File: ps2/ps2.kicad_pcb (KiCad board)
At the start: 2 copper layers, 135.9 x 48.9 mm, 40 parts, among them J1 keyboard, J2 perslot1a, J3 perslot1b, Q1 Q_NPN_CBE, Q2 Q_PNP_EBC, U1 74HC74, U10 74HC280, U11 74HC541, U2 74HC08, U3 74HC14, U4 74HC05, U5 74HC688, U6 74HC195, U7 74HC195, U8 74HC195, U9 74HC541

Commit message: applied sf68 & ps2 fixes stash from master
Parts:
- R7: value 20k -> 4k7
- moved R4 7.62 mm to (124.5, 81.3), turned to -90 degrees
- moved R8 7.62 mm to (124.5, 73.7), turned to 90 degrees
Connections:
- J1 pad 7: GND -> (no net)
- J1 pad 8: GND -> (no net)
- J1 pad 9: GND -> (no net)
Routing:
- net /DAT: track 65.2 -> 59.4 mm
- net /~{CLK}: track 31.6 -> 36.2 mm
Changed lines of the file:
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@@
 	(footprint "Resistor_THT:R_Axial_DIN0207_L6.3mm_D2.5mm_P2.54mm_Vertical"
 		(layer "F.Cu")
-		(at 124.46 81.28 -90)
+		(at 124.46 73.66 90)
 		(descr "Resistor, Axial_DIN0207 series, Axial, Vertical, pin pitch=2.54mm, 0.25W = 1/4W, length*diameter=6.3*2.5mm^2, http://cdn-reichelt.de/documents/datenblatt/B400/1_4W%23YAG.pdf")
 		(tags "Resistor Axial_DIN0207 series Axial Vertical pin pitch 2.54mm 0.25W = 1/4W length 6.3mm diameter 2.5mm")
 		(property "Reference" "R8"
-			(at -2.54 0 180)
+			(at -2.54 0 0)
 			(layer "F.SilkS")
 			(effects
@@
 		)
 		(property "Value" "4k7"
-			(at 1.27 2.37 90)
+			(at 1.27 2.37 270)
 			(layer "F.Fab")
 			(effects
@@
 		)
 		(property "Datasheet" ""
-			(at 0 0 90)
+			(at 0 0 270)
 			(layer "F.Fab")
 			(hide yes)
@@
 		)
 		(property "Description" ""
-			(at 0 0 90)
+			(at 0 0 270)
 			(layer "F.Fab")
 			(hide yes)
@@
 		)
 		(fp_text user "${REFERENCE}"
-			(at -2.54 0 180)
+			(at -2.54 0 0)
 			(layer "F.Fab")
 			(effects
@@
 		)
 		(pad "1" thru_hole circle
-			(at 0 0 270)
+			(at 0 0 90)
 			(size 1.6 1.6)
 			(drill 0.8)
@@
 		)
 		(pad "2" thru_hole circle
-			(at 2.54 0 270)
+			(at 2.54 0 90)
 			(size 1.6 1.6)
 			(drill 0.8)
@@
 			)
 		)
-		(property "Value" "20k"
+		(property "Value" "4k7"
 			(at 1.27 2.37 90)
 			(layer "F.Fab")
@@
 	(footprint "Resistor_THT:R_Axial_DIN0207_L6.3mm_D2.5mm_P2.54mm_Vertical"
 		(layer "F.Cu")
-		(at 124.46 73.66 90)
+		(at 124.46 81.28 -90)
 		(descr "Resistor, Axial_DIN0207 series, Axial, Vertical, pin pitch=2.54mm, 0.25W = 1/4W, length*diameter=6.3*2.5mm^2, http://cdn-reichelt.de/documents/datenblatt/B400/1_4W%23YAG.pdf")
 		(tags "Resistor Axial_DIN0207 series Axial Vertical pin pitch 2.54mm 0.25W = 1/4W length 6.3mm diameter 2.5mm")
 		(property "Reference" "R4"
-			(at 4.445 0 180)
+			(at 4.445 0 0)
 			(layer "F.SilkS")
 			(effects
@@
 		)
 		(property "Value" "4k7"
-			(at 1.27 2.37 90)
+			(at 1.27 2.37 270)
 			(layer "F.Fab")
 			(effects
@@
 		)
 		(property "Datasheet" ""
-			(at 0 0 90)
+			(at 0 0 270)
 			(layer "F.Fab")
 			(hide yes)
@@
 		)
 		(property "Description" ""
-			(at 0 0 90)
+			(at 0 0 270)
 			(layer "F.Fab")
 			(hide yes)
@@
 		)
 		(fp_text user "${REFERENCE}"
-			(at 4.445 0 180)
+			(at 4.445 0 0)
 			(layer "F.Fab")
 			(effects
@@
 		)
 		(pad "1" thru_hole circle
-			(at 0 0 90)
+			(at 0 0 270)
 			(size 1.6 1.6)
 			(drill 0.8)
@@
 		)
 		(pad "2" thru_hole circle
-			(at 2.54 0 90)
+			(at 2.54 0 270)
 			(size 1.6 1.6)
 			(drill 0.8)
@@
 		)
 		(pad "1" thru_hole circle
-			(at 0 0 90)
+			(at -2.6 0 90)
 			(size 1.509 1.509)
 			(drill 0.97)
@@
 		)
 		(pad "2" thru_hole circle
-			(at -2.6 0 90)
+			(at 0 0 90)
 			(size 1.509 1.509)
 			(drill 0.97)
@@
 		)
 		(pad "3" thru_hole circle
-			(at 2.05 0 90)
+			(at -4.65 0 90)
 			(size 1.509 1.509)
 			(drill 0.97)
@@
 		)
 		(pad "4" thru_hole circle
-			(at -4.65 0 90)
+			(at 2.05 0 90)
 			(size 1.509 1.509)
 			(drill 0.97)
@@
 		)
 		(pad "5" thru_hole circle
-			(at 2.05 2.49 90)
+			(at -4.65 2.49 90)
 			(size 1.509 1.509)
 			(drill 0.97)
@@
 		)
 		(pad "6" thru_hole circle
-			(at -4.65 2.49 90)
+			(at 2.05 2.49 90)
 			(size 1.509 1.509)
 			(drill 0.97)
@@
 			(layers "*.Cu" "*.Mask")
 			(remove_unused_layers no)
-			(net 10 "GND")
 		)
 		(pad "8" thru_hole circle
@@
 			(layers "*.Cu" "*.Mask")
 			(remove_unused_layers no)
-			(net 10 "GND")
 		)
 		(pad "9" thru_hole circle
@@
 			(layers "*.Cu" "*.Mask")
 			(remove_unused_layers no)
-			(net 10 "GND")
 		)
 		(embedded_fonts no)
@@
 	)
 	(segment
-		(start 124.46 66.04)
-		(end 125.73 67.31)
-		(width 0.2)
-		(layer "F.Cu")
-		(net 7)
-	)
-	(segment
 		(start 132.08 66.04)
 		(end 132.08 71.12)
@@
 	)
 	(segment
-		(start 125.73 67.31)
-		(end 125.73 72.39)
+		(start 124.46 81.28)
+		(end 115.98 81.28)
 		(width 0.2)
 		(layer "F.Cu")
@@
 	)
 	(segment
-		(start 124.46 73.66)
-		(end 115.98 73.66)
+		(start 124.46 66.04)
+		(end 125.73 64.77)
 		(width 0.2)
 		(layer "F.Cu")
@@
 	)
 	(segment
-		(start 124.46 66.04)
-		(end 125.73 64.77)
+		(start 130.81 64.77)
+		(end 132.08 66.04)
 		(width 0.2)
 		(layer "F.Cu")
@@
 	)
 	(segment
-		(start 115.98 73.66)
-		(end 115.52 74.12)
+		(start 115.98 81.28)
+		(end 115.52 80.82)
 		(width 0.2)
 		(layer "F.Cu")
@@
 	)
 	(segment
-		(start 125.73 72.39)
-		(end 124.46 73.66)
+		(start 132.08 71.12)
+		(end 128.27 74.93)
 		(width 0.2)
-		(layer "F.Cu")
+		(layer "B.Cu")
 		(net 7)
 	)
 	(segment
-		(start 130.81 64.77)
-		(end 132.08 66.04)
+		(start 128.27 74.93)
+		(end 128.27 77.47)
 		(width 0.2)
-		(layer "F.Cu")
+		(layer "B.Cu")
+		(net 7)
+	)
+	(segment
+		(start 128.27 77.47)
+		(end 124.46 81.28)
+		(width 0.2)
+		(layer "B.Cu")
 		(net 7)
 	)
@@
 	)
 	(segment
-		(start 154.94 81.28)
-		(end 153.67 82.55)
-		(width 0.2)
-		(layer "F.Cu")
-		(net 13)
-	)
-	(segment
-		(start 128.27 67.31)
-		(end 128.27 74.295)
-		(width 0.2)
-		(layer "F.Cu")
-		(net 13)
-	)
-	(segment
-		(start 113.06 76.2)
-		(end 113.03 76.17)
-		(width 0.2)
-		(layer "F.Cu")
-		(net 13)
-	)
-	(segment
-		(start 153.67 82.55)
-		(end 133.35 82.55)
+		(start 126.365 75.565)
+		(end 124.46 73.66)
 		(width 0.2)
 		(layer "F.Cu")
@@
 	)
 	(segment
-		(start 128.27 77.47)
-		(end 124.46 81.28)
+		(start 149.225 75.565)
+		(end 126.365 75.565)
 		(width 0.2)
 		(layer "F.Cu")
@@
 	)
 	(segment
-		(start 128.27 74.295)
-		(end 128.27 77.47)
+		(start 113.03 78.77)
+		(end 119.35 78.77)
 		(width 0.2)
 		(layer "F.Cu")
@@
 	)
 	(segment
-		(start 126.365 76.2)
-		(end 113.06 76.2)
+		(start 129.54 68.58)
+		(end 129.54 66.04)
 		(width 0.2)
 		(layer "F.Cu")
@@
 	)
 	(segment
-		(start 133.35 82.55)
-		(end 128.27 77.47)
+		(start 154.94 81.28)
+		(end 149.225 75.565)
 		(width 0.2)
 		(layer "F.Cu")
@@
 	)
 	(segment
-		(start 126.365 76.2)
-		(end 128.27 74.295)
+		(start 124.46 73.66)
+		(end 129.54 68.58)
 		(width 0.2)
 		(layer "F.Cu")
@@
 	)
 	(segment
-		(start 129.54 66.04)
-		(end 128.27 67.31)
+		(start 124.46 73.66)
+		(end 119.35 78.77)
 		(width 0.2)
 		(layer "F.Cu")

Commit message: [ps2] fixed send request RC constant 	t must be >= 100us 	RC was being t, therefore t was actually smaller than 100us 	RC is now >= 1.28 * 100us (R : 10kohm -> 14.7kohm) 	t ~= 120us >= 100us
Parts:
- R1: value 10k -> 14k7
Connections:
- J1 pad 7: (no net) -> GND
- J1 pad 8: (no net) -> GND
- J1 pad 9: (no net) -> GND
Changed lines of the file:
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@@
 			)
 		)
-		(property "Value" "10k"
+		(property "Value" "14k7"
 			(at 1.27 2.37 90)
 			(layer "F.Fab")
@@
 			(layers "*.Cu" "*.Mask")
 			(remove_unused_layers no)
+			(net 10 "GND")
 		)
 		(pad "8" thru_hole circle
@@
 			(layers "*.Cu" "*.Mask")
 			(remove_unused_layers no)
+			(net 10 "GND")
 		)
 		(pad "9" thru_hole circle
@@
 			(layers "*.Cu" "*.Mask")
 			(remove_unused_layers no)
+			(net 10 "GND")
 		)
 		(embedded_fonts no)

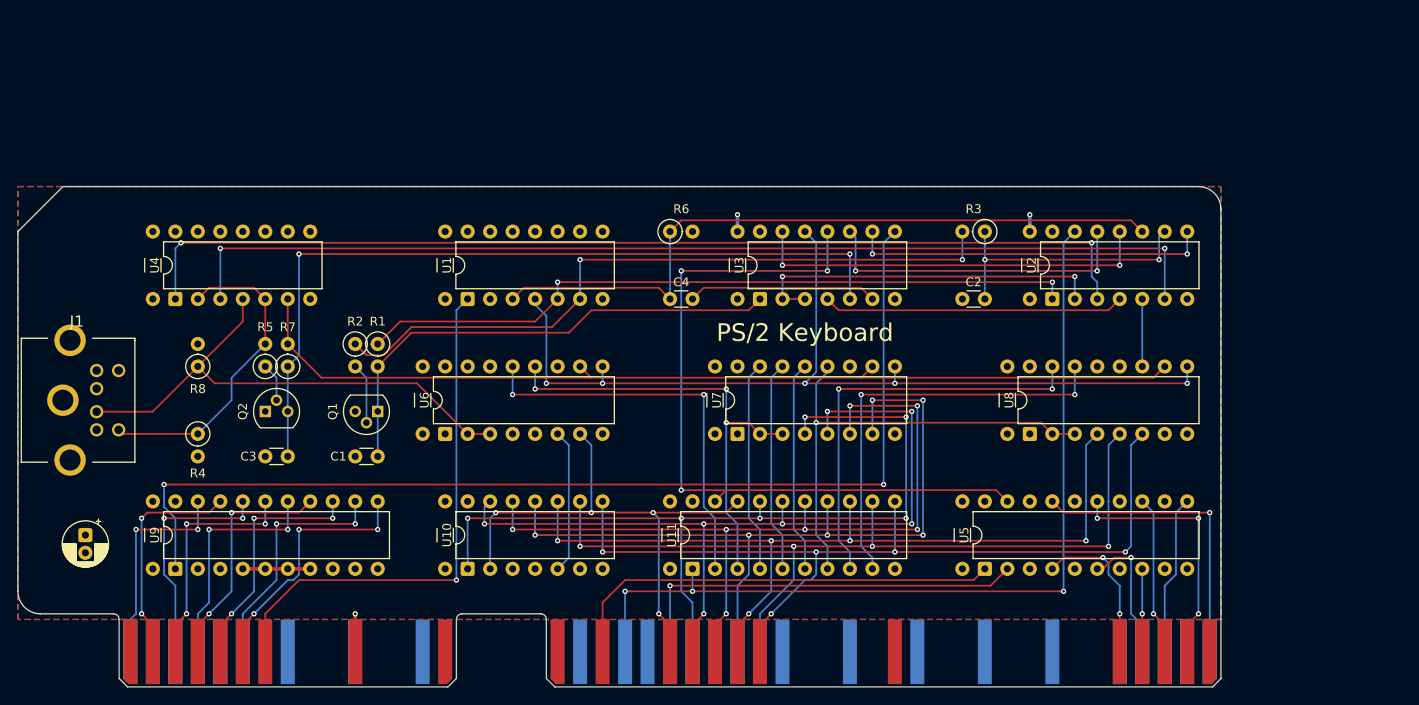
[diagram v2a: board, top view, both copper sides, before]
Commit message: [ps2]:	made pcb design of the new latest schematic
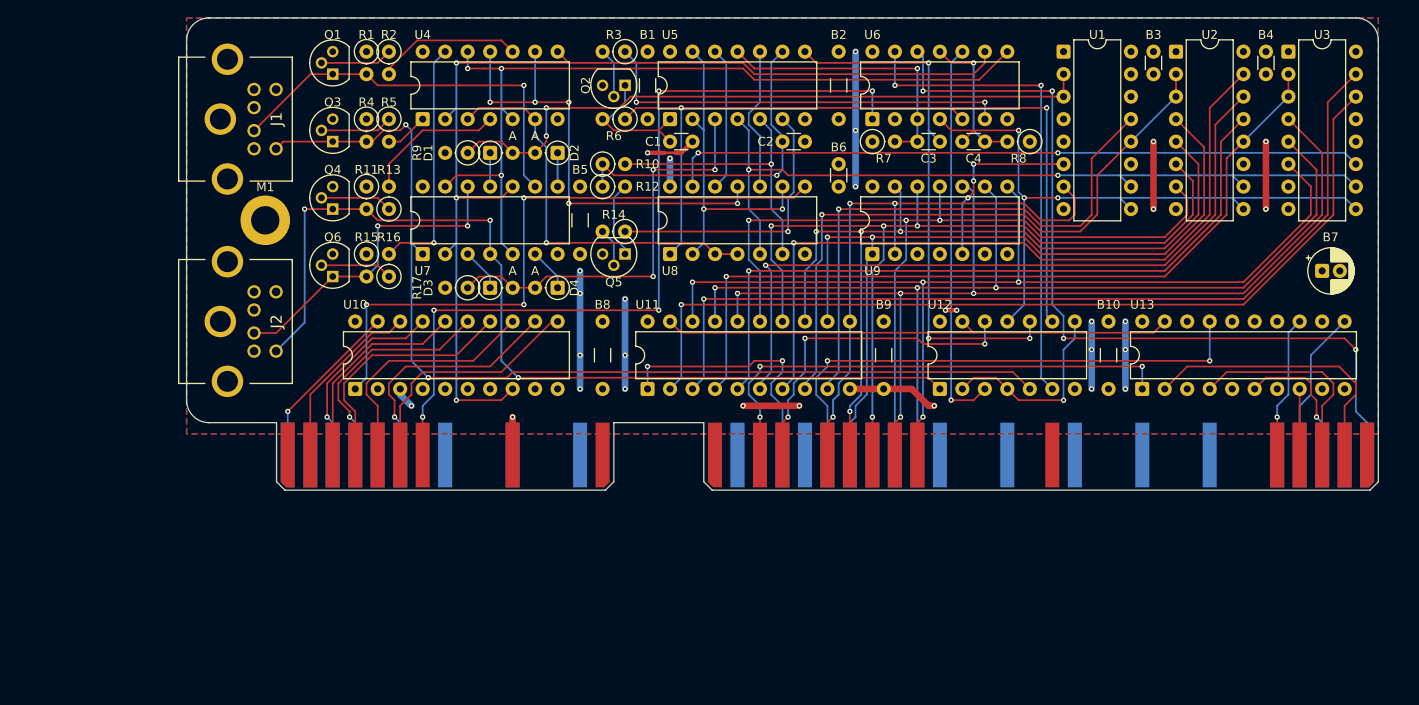
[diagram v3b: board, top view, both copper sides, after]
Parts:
- removed CB1 (x11): C_Disc_D3.0mm_W1.6mm_P7.62mm, Capacitor_THT:C_Disc_D3.0mm_W1.6mm_P7.62mm
- removed CB1: CP_Radial_D5.0mm_P2.00mm, Capacitor_THT:CP_Radial_D5.0mm_P2.00mm
- added B1: 100n, Capacitor_THT:C_Disc_D3.0mm_W1.6mm_P7.62mm, F.Cu at (175.3, 38.1)
- added B10: 100n, Capacitor_THT:C_Disc_D3.0mm_W1.6mm_P7.62mm, F.Cu at (227.3, 68.6)
- added B2: 100n, Capacitor_THT:C_Disc_D3.0mm_W1.6mm_P7.62mm, F.Cu at (196.8, 38.1)
- added B3: 100n, Capacitor_THT:C_Disc_D3.0mm_W1.6mm_P2.54mm, F.Cu at (232.4, 38.1)
- added B4: 100n, Capacitor_THT:C_Disc_D3.0mm_W1.6mm_P2.54mm, F.Cu at (245.1, 38.1)
- added B5: 100n, Capacitor_THT:C_Disc_D3.0mm_W1.6mm_P7.62mm, F.Cu at (167.6, 53.3)
- added B6: 100n, Capacitor_THT:C_Disc_D3.0mm_W1.6mm_P2.54mm, F.Cu at (196.8, 53.3)
- added B7: 10u, Capacitor_THT:CP_Radial_D5.0mm_P2.00mm, F.Cu at (251.5, 62.9)
- added B8: 100n, Capacitor_THT:C_Disc_D3.0mm_W1.6mm_P7.62mm, F.Cu at (170.2, 68.6)
- added B9: 100n, Capacitor_THT:C_Disc_D3.0mm_W1.6mm_P7.62mm, F.Cu at (201.9, 68.6)
- added D1: schotty, Diode_THT:D_DO-35_SOD27_P2.54mm_Vertical_AnodeUp, F.Cu at (157.5, 49.5)
- added D2: schotty, Diode_THT:D_DO-35_SOD27_P2.54mm_Vertical_AnodeUp, F.Cu at (165.1, 49.5)
- added D3: schotty, Diode_THT:D_DO-35_SOD27_P2.54mm_Vertical_AnodeUp, F.Cu at (157.5, 64.8)
- added D4: schotty, Diode_THT:D_DO-35_SOD27_P2.54mm_Vertical_AnodeUp, F.Cu at (165.1, 64.8)
- added J4: perslot1a, Connector_PCBEdge:pcb_edge_60_P2.54_new, F.Cu at (181.6, 80.0)
- added M1: MountingHole_3.2mm_M3_DIN965_Pad, MountingHole:MountingHole_3.2mm_M3_DIN965_Pad, F.Cu at (132.1, 57.1)
- added Q3: BC547B, Package_TO_SOT_THT:TO-92, F.Cu at (139.7, 48.3)
- added Q4: BC547B, Package_TO_SOT_THT:TO-92, F.Cu at (139.7, 55.9)
- added Q5: BC547B, Package_TO_SOT_THT:TO-92, F.Cu at (172.7, 61.0)
- added Q6: BC547B, Package_TO_SOT_THT:TO-92, F.Cu at (139.7, 63.5)
- added R10: 10k, Resistor_THT:R_Axial_DIN0207_L6.3mm_D2.5mm_P2.54mm_Vertical, F.Cu at (170.2, 50.8)
- added R11: 4k7, Resistor_THT:R_Axial_DIN0207_L6.3mm_D2.5mm_P2.54mm_Vertical, F.Cu at (143.5, 53.3)
- added R12: 1k, Resistor_THT:R_Axial_DIN0207_L6.3mm_D2.5mm_P2.54mm_Vertical, F.Cu at (170.2, 53.3)
- added R13: 10k, Resistor_THT:R_Axial_DIN0207_L6.3mm_D2.5mm_P2.54mm_Vertical, F.Cu at (146.1, 55.9)
- added R14: 10k, Resistor_THT:R_Axial_DIN0207_L6.3mm_D2.5mm_P2.54mm_Vertical, F.Cu at (172.7, 58.4)
- added R15: 4k7, Resistor_THT:R_Axial_DIN0207_L6.3mm_D2.5mm_P2.54mm_Vertical, F.Cu at (143.5, 61.0)
- added R16: 10k, Resistor_THT:R_Axial_DIN0207_L6.3mm_D2.5mm_P2.54mm_Vertical, F.Cu at (146.1, 63.5)
- added R17: 10k, Resistor_THT:R_Axial_DIN0207_L6.3mm_D2.5mm_P2.54mm_Vertical, F.Cu at (154.9, 64.8)
- added R9: 10k, Resistor_THT:R_Axial_DIN0207_L6.3mm_D2.5mm_P2.54mm_Vertical, F.Cu at (154.9, 49.5)
- added U12: 74HC32, Package_DIP:DIP-14_W7.62mm, F.Cu at (208.3, 76.2)
- added U13: 74HC688, Package_DIP:DIP-20_W7.62mm, F.Cu at (231.1, 76.2)
- C1: value 10nF -> 10n
- C2: value 22pF -> 10n
- C3: value 10nF -> 220p
- C4: value 22pF -> 22p
- J1: value keyboard -> port0
- J2: value perslot1a -> port1; footprint Connector_PCBEdge:pcb_edge_60_P2.54_new -> Connector_TE-Connectivity:57492651
- Q1: value Q_NPN_CBE -> BC547B
- Q2: value Q_PNP_EBC -> BC547B
- R1: value 14k7 -> 4k7
- R6: value 10k -> 14k7
- R7: value 4k7 -> 1k
- R8: value 4k7 -> 2k
- U1: value 74HC74 -> 74HC195; footprint Package_DIP:DIP-14_W7.62mm -> Package_DIP:DIP-16_W7.62mm
- U10: value 74HC280 -> 74HC541; footprint Package_DIP:DIP-14_W7.62mm -> Package_DIP:DIP-20_W7.62mm
- U2: value 74HC08 -> 74HC195; footprint Package_DIP:DIP-14_W7.62mm -> Package_DIP:DIP-16_W7.62mm
- U3: value 74HC14 -> 74HC195; footprint Package_DIP:DIP-14_W7.62mm -> Package_DIP:DIP-16_W7.62mm
- U4: value 74HC05 -> 74HC02
- U5: value 74HC688 -> 74HC14; footprint Package_DIP:DIP-20_W7.62mm -> Package_DIP:DIP-14_W7.62mm
- U6: value 74HC195 -> 74HC74; footprint Package_DIP:DIP-16_W7.62mm -> Package_DIP:DIP-14_W7.62mm
- U7: value 74HC195 -> 74HC32; footprint Package_DIP:DIP-16_W7.62mm -> Package_DIP:DIP-14_W7.62mm
- U8: value 74HC195 -> 74HC00; footprint Package_DIP:DIP-16_W7.62mm -> Package_DIP:DIP-14_W7.62mm
- U9: value 74HC541 -> 74HC280; footprint Package_DIP:DIP-20_W7.62mm -> Package_DIP:DIP-14_W7.62mm
- moved R8 97.4 mm to (218.4, 48.3), turned to 180 degrees
- moved U9 86.4 mm to (200.7, 61.0)
- moved C3 81.8 mm to (205.7, 48.3)
- moved U1 72.9 mm to (222.2, 38.1), turned to 0 degrees
- moved R7 70.8 mm to (200.7, 48.3), turned to 0 degrees
- moved U3 65.9 mm to (247.7, 38.1), turned to 0 degrees
- moved U5 62.0 mm to (177.8, 45.7)
- moved U6 59.9 mm to (200.7, 45.7)
- moved Q2 54.8 mm to (172.7, 41.9), turned to 180 degrees
- moved C1 50.3 mm to (177.8, 48.3)
- moved J2 48.1 mm to (130.8, 67.3), turned to 90 degrees
- moved R3 45.4 mm to (172.7, 38.1)
- moved U8 45.4 mm to (177.8, 61.0)
- moved U7 41.0 mm to (149.9, 61.0)
- moved R4 40.3 mm to (143.5, 45.7)
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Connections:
- C1 pad 1: GND -> Net-(Q5-C)
- C1 pad 2: Net-(Q1-C) -> GND
- C2 pad 1: GND -> Net-(C4-Pad1)
- C2 pad 2: Net-(C2-Pad2) -> GND
- C3 pad 1: GND -> Net-(U1A-C)
- C3 pad 2: Net-(Q2-C) -> /TBSY
- C4 pad 1: Net-(U1A-C) -> /~{W}
- C4 pad 2: Net-(C4-Pad2) -> Net-(U1B-C)
- J1 pad 1: /DAT -> /DAT_{0}
- J1 pad 5: /~{CLK} -> /~{CLK_{0}}
- J2 pad 1: +5V -> /DAT_{1}
- J2 pad 4: GND -> +5V
- J2 pad 5: /DS.~{U} -> /~{CLK_{1}}
- J2 pad 8: /DIR.~{R} -> GND
- Q1 pad 1: Net-(Q1-C) -> /DAT_{0}
- Q1 pad 2: Net-(Q1-B) -> Net-(Q2-B)
- Q2 pad 1: +5V -> Net-(Q5-C)
- Q2 pad 2: Net-(Q2-B) -> Net-(Q5-B)
- Q2 pad 3: Net-(Q2-C) -> GND
- R1 pad 1: Net-(U1A-Q) -> +5V
- R1 pad 2: Net-(Q1-C) -> /DAT_{0}
- R2 pad 1: Net-(U1A-~{Q}) -> Net-(Q2-B)
- R2 pad 2: Net-(Q1-B) -> Net-(R5-Pad2)
- R3 pad 1: Net-(C2-Pad2) -> Net-(U1A-~{Q})
- R3 pad 2: Net-(U1A-~{Q}) -> Net-(Q5-B)
- R4 pad 1: /~{CLK} -> +5V
- R4 pad 2: +5V -> /~{CLK_{0}}
- R5 pad 1: Net-(Q2-B) -> Net-(Q1-B)
- R5 pad 2: /~{CLK} -> Net-(R4-Pad2)
- R6 pad 1: Net-(U1A-C) -> /SBSY
- R6 pad 2: GND -> Net-(Q5-C)
- R7 pad 1: Net-(Q2-C) -> +5V
- R7 pad 2: /CP -> Net-(U1A-C)
- R8 pad 1: /DAT -> +5V
- R8 pad 2: +5V -> Net-(U1B-C)
- U1 pad 1: /~{RES} -> +5V
- U1 pad 10: +5V -> /CP
- U1 pad 11: GND -> unconnected-(U9-~{Q3}-Pad11)
- U1 pad 12: GND -> /shift_registers/D_{q6}
- U1 pad 13: +5V -> /shift_registers/D_{q7}
- U1 pad 14: +5V -> unconnected-(U9-Q1-Pad14)
- U1 pad 2: GND -> /DAT_{d}
- U1 pad 3: Net-(U1A-C) -> /DAT_{d}
- U1 pad 4: /~{W} -> +5V
- U1 pad 5: Net-(U1A-Q) -> +5V
- U1 pad 6: Net-(U1A-~{Q}) -> /shift_registers/EPAR
- U1 pad 7: GND -> /D_{15}
- U1 pad 8: unconnected-(U1B-~{Q}-Pad8) -> GND
- U1 pad 9: unconnected-(U1B-Q-Pad9) -> /~{W}
- U10 pad 1: /D_{14} -> /~{RCV}
- U10 pad 10: /D_{10} -> GND
- U10 pad 11: /D_{11} -> /IRQ_{0}
- U10 pad 12: /D_{12} -> /IRQ_{1}
- U10 pad 13: /D_{13} -> /IRQ_{2}
- U10 pad 14: +5V -> /IRQ_{3}
- U10 pad 2: /D_{15} -> GND
- U10 pad 3: unconnected-(U10-NC-Pad3) -> +5V
- U10 pad 5: /PAR -> GND
- U10 pad 6: unconnected-(U10-Odd-Pad6) -> GND
- U10 pad 8: /D_{8} -> /PORT
- U10 pad 9: /D_{9} -> +5V
- U11 pad 11: /D_{8} -> /D_{15}
- U11 pad 12: /D_{9} -> /D_{14}
- U11 pad 13: /D_{10} -> /D_{13}
- U11 pad 14: /D_{11} -> /D_{12}
- U11 pad 15: /D_{12} -> /D_{11}
- U11 pad 16: /D_{13} -> /D_{10}
- U11 pad 17: /D_{14} -> /D_{9}
- U11 pad 18: /D_{15} -> /D_{8}
- U11 pad 2: /DQ_{7} -> /shift_registers/D_{q0}
- U11 pad 3: /DQ_{6} -> /shift_registers/D_{q1}
- U11 pad 4: /DQ_{5} -> /shift_registers/D_{q2}
- U11 pad 5: /DQ_{4} -> /shift_registers/D_{q3}
- U11 pad 6: /DQ_{3} -> /shift_registers/D_{q4}
- U11 pad 7: /DQ_{2} -> /shift_registers/D_{q5}
- U11 pad 8: /DQ_{1} -> /shift_registers/D_{q6}
- U11 pad 9: /DQ_{0} -> /shift_registers/D_{q7}
- U2 pad 1: Net-(U1A-Q) -> +5V
- U2 pad 10: Net-(U1A-C) -> /CP
- U2 pad 11: Net-(U2-Pad11) -> unconnected-(U10-~{Q3}-Pad11)
- U2 pad 12: Net-(U2-Pad12) -> /shift_registers/D_{q2}
- U2 pad 13: /DIR.~{R} -> /shift_registers/D_{q3}
- U2 pad 14: +5V -> /shift_registers/D_{q4}
- U2 pad 2: Net-(U2-Pad2) -> /shift_registers/D_{q6}
- U2 pad 3: Net-(U2-Pad3) -> /shift_registers/D_{q6}
- U2 pad 4: Net-(U2-Pad4) -> /D_{14}
- U2 pad 5: /~{DQO} -> /D_{13}
- U2 pad 6: Net-(U2-Pad6) -> /D_{12}
- U2 pad 7: GND -> /D_{11}
- U2 pad 8: Net-(U2-Pad8) -> GND
- U2 pad 9: Net-(C2-Pad2) -> /~{W}
- U3 pad 1: Net-(Q1-C) -> +5V
- U3 pad 10: Net-(U2-Pad12) -> /CP
- U3 pad 11: /~{S} -> /~{D_{q}}
- U3 pad 12: /~{W} -> unconnected-(U11-Q3-Pad12)
- U3 pad 13: Net-(U2-Pad11) -> unconnected-(U11-Q2-Pad13)
- U3 pad 14: +5V -> /shift_registers/D_{q0}
- U3 pad 2: Net-(U2-Pad2) -> /shift_registers/D_{q2}
- U3 pad 3: Net-(U2-Pad2) -> /shift_registers/D_{q2}
- U3 pad 4: Net-(U2-Pad4) -> /D_{10}
- U3 pad 5: Net-(Q2-C) -> /D_{9}
- U3 pad 6: Net-(C4-Pad2) -> /D_{8}
- U3 pad 8: /~{RCV} -> GND
- U3 pad 9: Net-(U2-Pad8) -> /~{W}
- U4 pad 1: Net-(U2-Pad3) -> Net-(R4-Pad2)
- U4 pad 10: unconnected-(U4-Pad10) -> Net-(R5-Pad2)
- U4 pad 11: GND -> /DAT_{h}
- U4 pad 12: unconnected-(U4-Pad12) -> /ports_mux/~{P_{1}}
- U4 pad 13: GND -> Net-(R11-Pad2)
- U4 pad 2: /~{CLK} -> /PORT
- U4 pad 3: Net-(U2-Pad6) -> /~{CLK_{h}}
- U4 pad 4: /DAT -> Net-(R10-Pad2)
- U4 pad 5: /~{CLK} -> /ports_mux/~{P_{1}}
- U4 pad 6: /CP -> /~{CLK_{h}}
- U4 pad 8: unconnected-(U4-Pad8) -> /PORT
- U4 pad 9: GND -> /DAT_{h}
- U5 pad 1: /DS.~{U} -> Net-(Q5-C)
- U5 pad 10: GND -> Net-(U7-Pad10)
- U5 pad 11: /A_{4} -> Net-(U1A-C)
- U5 pad 12: GND -> Net-(U7-Pad12)
- U5 pad 13: /A_{3} -> Net-(U7-Pad2)
- U5 pad 14: GND -> +5V
- U5 pad 2: /BE.~{IO} -> Net-(U7-Pad2)
- U5 pad 3: GND -> /~{CLK_{d}}
- U5 pad 4: /A_{7} -> /CP
- U5 pad 5: GND -> Net-(R15-Pad2)
- U5 pad 6: /A_{6} -> Net-(R17-Pad1)
- U5 pad 8: /A_{5} -> /TBSY
- U5 pad 9: GND -> Net-(C4-Pad1)
- U6 pad 1: +5V -> /~{RES}
- U6 pad 10: /CP -> Net-(U1B-~{S})
- U6 pad 11: unconnected-(U6-~{Q3}-Pad11) -> Net-(U1B-C)
- U6 pad 12: /DQ_{6} -> /A_{1}
- U6 pad 13: /DQ_{7} -> Net-(U1B-~{R})
- U6 pad 14: unconnected-(U6-Q1-Pad14) -> +5V
- U6 pad 2: /DAT -> GND
- U6 pad 3: /DAT -> Net-(U1A-C)
- U6 pad 4: +5V -> /~{W}
- U6 pad 5: +5V -> /SBSY
- U6 pad 6: /PAR -> Net-(U1A-~{Q})
- U6 pad 7: /D_{15} -> GND
- U6 pad 8: GND -> /ports_mux/~{P_{1}}
- U6 pad 9: /~{W} -> /PORT
- U7 pad 1: +5V -> /~{CLK_{0}}
- U7 pad 10: /CP -> /PORT
- U7 pad 11: unconnected-(U7-~{Q3}-Pad11) -> Net-(D4-K)
- U7 pad 12: /DQ_{2} -> /DAT_{1}
- U7 pad 13: /DQ_{3} -> /ports_mux/~{P_{1}}
- U7 pad 14: /DQ_{4} -> +5V
- U7 pad 2: /DQ_{6} -> /PORT
- U7 pad 3: /DQ_{6} -> Net-(D1-K)
- U7 pad 4: /D_{14} -> /~{CLK_{1}}
- U7 pad 5: /D_{13} -> /ports_mux/~{P_{1}}
- U7 pad 6: /D_{12} -> Net-(D3-K)
- U7 pad 7: /D_{11} -> GND
- U7 pad 8: GND -> Net-(D2-K)
- U7 pad 9: /~{W} -> /DAT_{0}
- U8 pad 1: +5V -> /SBSY
- U8 pad 10: /CP -> Net-(U7-Pad10)
- U8 pad 11: /~{DQO} -> /DAT_{h}
- U8 pad 12: unconnected-(U8-Q3-Pad12) -> Net-(U7-Pad12)
- U8 pad 13: unconnected-(U8-Q2-Pad13) -> /~{D_{q}}
- U8 pad 14: /DQ_{0} -> +5V
- U8 pad 2: /DQ_{2} -> Net-(U7-Pad2)
- U8 pad 3: /DQ_{2} -> /~{CLK_{h}}
- U8 pad 4: /D_{10} -> /~{CLK_{h}}
- U8 pad 5: /D_{9} -> /CP
- U8 pad 6: /D_{8} -> Net-(R15-Pad2)
- U8 pad 8: GND -> /~{RCV}
- U8 pad 9: /~{W} -> Net-(U7-Pad2)
- U9 pad 1: /~{RCV} -> /D_{14}
- U9 pad 10: GND -> /D_{10}
- U9 pad 11: /IRQ_{0} -> /D_{11}
- U9 pad 12: /IRQ_{1} -> /D_{12}
- U9 pad 13: /IRQ_{2} -> /D_{13}
- U9 pad 14: /IRQ_{3} -> +5V
- U9 pad 2: GND -> /D_{15}
- U9 pad 3: +5V -> unconnected-(U12-NC-Pad3)
- U9 pad 5: GND -> /shift_registers/EPAR
- U9 pad 6: GND -> unconnected-(U12-Odd-Pad6)
- U9 pad 8: GND -> /D_{8}
- U9 pad 9: +5V -> /D_{9}
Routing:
- net /PORT: track 0.00 -> 119.9 mm, vias 0 -> 3
- net Net-(U2-Pad6): track 118.1 -> 0.00 mm, vias 2 -> 0
- net /~{CLK_{0}}: track 0.00 -> 116.2 mm, vias 0 -> 2
- net Net-(U2-Pad3): track 116.1 -> 0.00 mm, vias 2 -> 0
- net /~{CLK_{1}}: track 0.00 -> 106.1 mm, vias 0 -> 3
- net /shift_registers/D_{q1}: track 0.00 -> 102.3 mm, vias 0 -> 1
- net /shift_registers/D_{q0}: track 0.00 -> 102.3 mm, vias 0 -> 1
- net /ports_mux/~{P_{1}}: track 0.00 -> 94.9 mm, vias 0 -> 3
- net /shift_registers/D_{q2}: track 0.00 -> 91.4 mm, vias 0 -> 1
- net /SBSY: track 0.00 -> 91.4 mm, vias 0 -> 2
- net Net-(Q2-C): track 90.7 -> 0.00 mm, vias 2 -> 0
- net /shift_registers/D_{q5}: track 0.00 -> 84.4 mm, vias 0 -> 1
- net /shift_registers/D_{q4}: track 0.00 -> 82.6 mm, vias 0 -> 1
- net Net-(U1A-Q): track 82.1 -> 0.00 mm, vias 2 -> 0
- net /shift_registers/D_{q3}: track 0.00 -> 81.7 mm, vias 0 -> 1
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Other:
- board size 135.9 x 48.9 mm -> 134.6 x 45.7 mm
- board text removed: "PS/2 Keyboard"

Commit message: [ps2]	changed fingers footprints
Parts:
- added G***: LOGO, LOGO, B.Cu at (245.1, 62.2)
- J3: footprint Connector_PCBEdge:pcb_edge_30_P2.54_new -> Connector_PCBEdge:edge_connector_15p_2.54mm
- J4: footprint Connector_PCBEdge:pcb_edge_60_P2.54_new -> Connector_PCBEdge:edge_connector_30p_2.54mm
- moved B1 1.27 mm to (176.5, 38.1)
- moved B2 1.27 mm to (198.1, 38.1)
- moved B3 1.27 mm to (233.7, 38.1)
- moved B5 1.27 mm to (168.9, 53.3)
- moved B6 1.27 mm to (198.1, 53.3)
- moved C2 1.27 mm to (191.8, 48.3)
- moved C4 1.27 mm to (212.1, 48.3)
- moved D1 1.27 mm to (158.8, 49.5)
- moved D2 1.27 mm to (166.4, 49.5)
- moved D3 1.27 mm to (158.8, 64.8)
- moved D4 1.27 mm to (166.4, 64.8)
- moved Q1 1.27 mm to (141.0, 40.6)
- moved Q2 1.27 mm to (174.0, 41.9)
- moved Q3 1.27 mm to (141.0, 48.3)
- moved Q4 1.27 mm to (141.0, 55.9)
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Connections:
- J1 pad 7: GND -> (no net)
- J1 pad 8: GND -> (no net)
- J1 pad 9: GND -> (no net)
- J2 pad 7: GND -> (no net)
- J2 pad 8: GND -> (no net)
- J2 pad 9: GND -> (no net)
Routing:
- net /DAT_{1}: track 36.2 -> 37.5 mm
- net /DAT_{0}: track 45.6 -> 46.9 mm
- net /~{CLK_{0}}: track 116.2 -> 117.4 mm
- net /~{CLK_{1}}: track 106.1 -> 106.6 mm
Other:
- board size 134.6 x 45.7 mm -> 137.2 x 45.7 mm
- board text added: "Copyright © 2026 Pietro Senesi, Italy"
- board text added: "Dual-port Extension"
- board text added: "PS/2"
